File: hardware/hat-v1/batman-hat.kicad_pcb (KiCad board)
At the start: 4 copper layers, 65 x 56.5 mm, 174 parts, among them J1 BATT pads, J2 Pi 40-pin (female, 11 mm stac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, J3 mPCIe 5.2H, J4 U.FL, J5 Tag-Connect TC2050, J6 PANEL BTN, Q1 CSD19537Q3, Q10 BSS138, Q11 Si2301CDS, Q12 BSS138, Q2 BSS138, Q3 CSD17578Q3A, Q6 BSS138, Q7 BSS138, U1 TPS26631RGER, U11 SLB9672XU2.0, U12 ATECC608C-TFLXTLS, U13 RV-3028-C7, U14 MAX-M10S-00B, U15 OPA333AIDBVR, U2 INA226AIDGSR, U3 LMR33640DDDAR, U4 LM74700QDBVRQ1, U7 TPS62933FDRLR, U8 INA226AIDGSR, U9 LTC2955ITS8-2#TRPBF

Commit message: HAT v1 layout: remove_dangling() cleans rip-up leftovers after each SES import
Co-Authored-By: Claude Opus 5.5 <noreply@anthropic.com>
Claude-Session: https://claude.ai/code/session_01MLRuxTEmuMV82xcNLE62jW
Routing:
- net HALOW_RESET_N: track 59.4 -> 46.4 mm
- net VCC_5V: track 9.52 -> 1.95 mm
- net PG_5V: track 31.9 -> 24.4 mm
- net EF_OUT: track 37.2 -> 30.2 mm
- net VSYS: track 154.9 -> 151.3 mm
- net 3V3_SEC: track 140.5 -> 138.3 mm
- net TPM_PIRQ_N: track 48.2 -> 46.8 mm
- net BAT_PRESENT_N: track 42.2 -> 41.4 mm
- net KILL_REQ: track 30.2 -> 29.6 mm

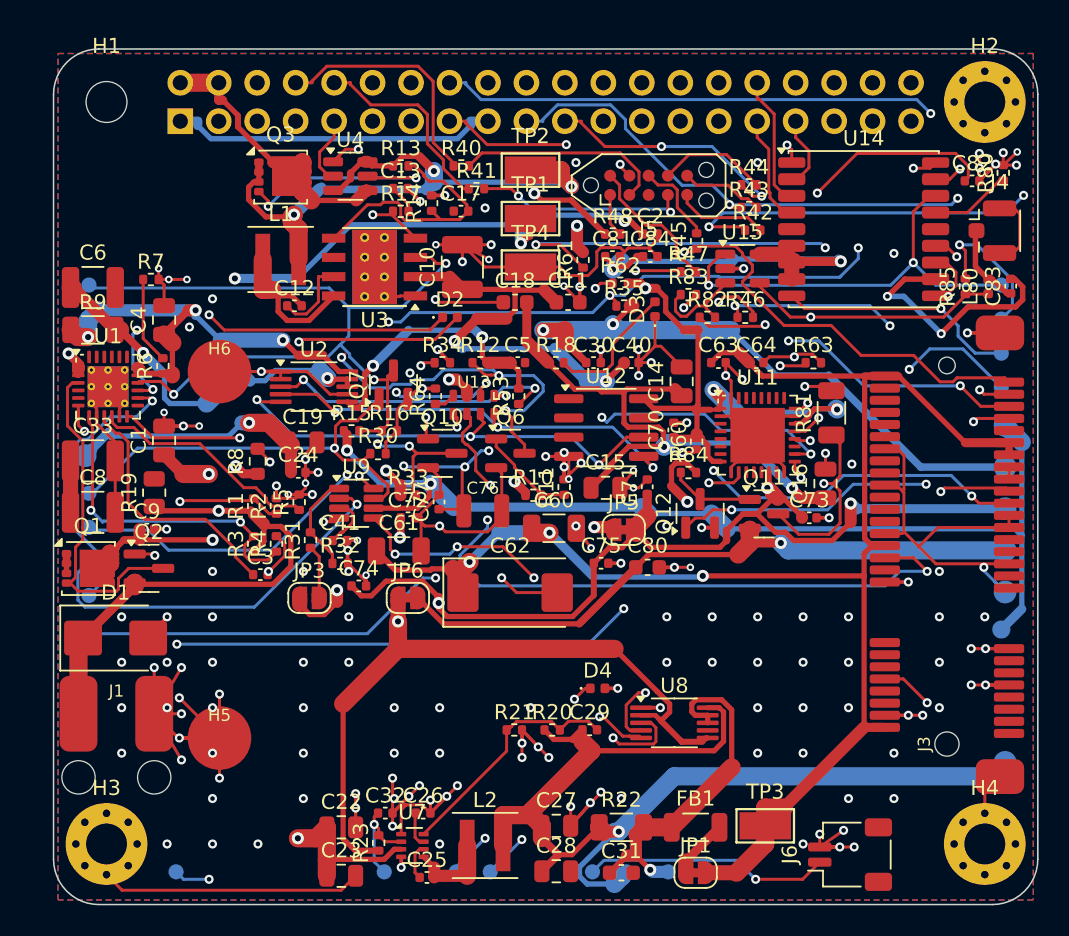
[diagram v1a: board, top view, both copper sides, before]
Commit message: HAT v1: routing close-out - 0 unconnected; input stage re-placed
Local take-over of the cloud hand-off (8041361, 10 unconnected):
- short breaks fixed by hand edits (SPI1_SCLK, J5.3/C16.2 GND islands,
  VCC_5V / 5V_BUCK / PG_5V, HALOW_RESET_N re-routed pin to pin)
- eFuse column was a placement problem, not a routing one: Q1 source pins
  (full battery current, ~3.5 A at 2S low) faced the board edge with room
  for one 0.3 mm via; U1 pins 3-5 were trapped in a 0.77 mm edge strip.
  U1 and Q1 rotated 90 deg, main current on F pours (J1->D1->Q1,
  Q1->U1 IN, U1 OUT->R9), VBAT_RAW distribution on an In2 pour with a
  track keep-out, hand lanes for U1's fixed pin order, damper re-stacked
- remaining connections by Freerouting 2.1.0 (GUI mode, 12 passes)
- U1 EP vias / J2.25 solid zone connection (starved_thermal), dangling
  leftovers removed only where KiCad connectivity stays unchanged

DRC (pcbnew.WriteDRCReport): 0 unconnected, 0 clearance / hole / mask /
starved-thermal errors; left: items_not_allowed x2 (H1, pending Pi 4
drawing) and 6 bridge-type dangling-track warnings.

Replayable scripts in hardware/hat-v1/closeout (run.sh); Freerouting is not
deterministic, run.sh gates on 0 unconnected. Not addressed yet: main power
paths bottleneck at 0.35 mm (VSYS->U3, 5V_BUCK, 5V_PI->J2, 3V3_BUCK),
already so on the cloud board - next step.

Refs #47, #91, #122

Co-Authored-By: Claude Opus 5.5 <noreply@anthropic.com>
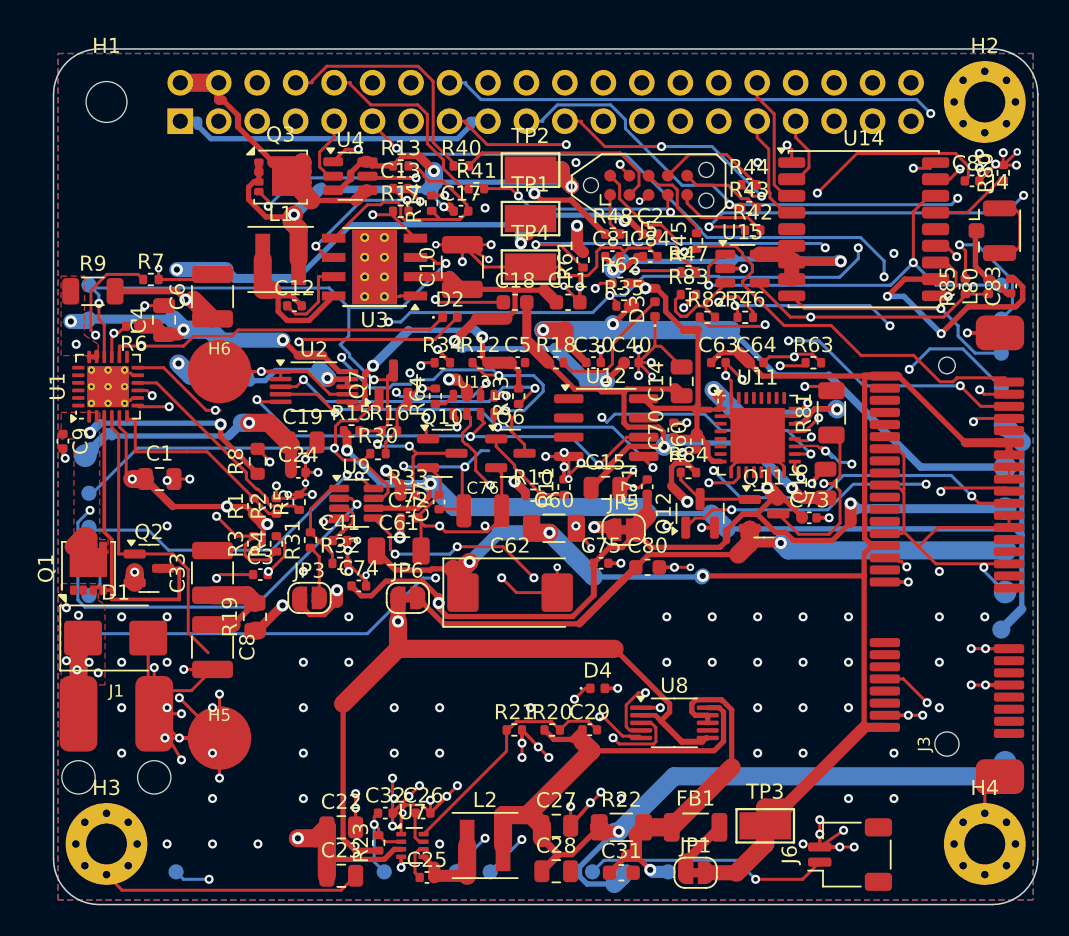
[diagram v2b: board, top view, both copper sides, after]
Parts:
- moved C8 11.9 mm to (110.5, 139.5), turned to -90 degrees
- moved C33 10.8 mm to (110.5, 134.6), turned to 90 degrees
- moved R19 10.6 mm to (113.3, 137.5)
- moved C9 8.03 mm to (100.6, 125.9), turned to -90 degrees
- moved C6 7.92 mm to (110.5, 116.3), turned to 90 degrees
- moved R6 3.26 mm to (105.3, 118.3), turned to 180 degrees
- moved C1 2.57 mm to (107.0, 128.4), turned to 0 degrees
- moved R9 2.55 mm to (102.6, 116.0)
- turned Q1 to 90 degrees
- turned U1 to 90 degrees
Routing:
- net EF_IN: track 39.9 -> 16.1 mm, vias 3 -> 2
- net EF_DRV: track 38.3 -> 20.3 mm, vias 3 -> 0
- net PG_5V: track 24.4 -> 41.4 mm
- net HALOW_RESET_N: track 46.4 -> 60.3 mm, vias 2 -> 3
- net GND: track 332.3 -> 343.3 mm, vias 169 -> 171
- net EN_5V: track 55.7 -> 45.4 mm
- net VCC_5V: track 1.95 -> 11.0 mm, vias 0 -> 2
- net EF_OUT: track 30.2 -> 23.7 mm
- net SPI1_SCLK: track 26.9 -> 31.8 mm, vias 1 -> 2
- net EF_OVP: track 21.9 -> 17.6 mm
- net VBAT_RAW: track 108.5 -> 104.3 mm, vias 6 -> 15
- net EF_UVLO: track 17.6 -> 13.9 mm, vias 2 -> 0
- net VBAT_DAMP: track 3.40 -> 6.41 mm
- net 5V_BUCK: track 100.7 -> 102.9 mm, vias 5 -> 6
- net EF_SHDN: track 41.0 -> 43.0 mm
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- added copper zone on F.Cu, net EF_IN
- added copper zone on F.Cu, net EF_OUT
- added copper zone on F.Cu, net VBAT_RAW
- added copper zone on In2.Cu, net VBAT_RAW
